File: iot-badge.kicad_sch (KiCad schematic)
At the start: 12 parts, among them J1 USB_C_Receptacle_USB2.0, J11 Conn_01x01_Male, J12 Conn_01x01_Male, SW1 SW_Push, SW2 SW_Push, SW3 SW_Push, SW4 SW_Push, SW5 SW_Push, SW6 SW_Push, U1 ESP32-WROOM-32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

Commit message: started readme
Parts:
- BT1: footprint Battery:BatteryHolder_Keystone_3009_1x2450 -> Battery:BatteryHolder_Keystone_1057_1x2032
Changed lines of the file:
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@@
       (effects (font (size 1.27 1.27)) (justify left))
     )
-    (property "Footprint" "Battery:BatteryHolder_Keystone_3009_1x2450" (id 2) (at 76.2 108.966 90)
+    (property "Footprint" "Battery:BatteryHolder_Keystone_1057_1x2032" (id 2) (at 76.2 108.966 90)
       (effects (font (size 1.27 1.27)) hide)
     )
@@
   (symbol_instances
     (path "/2b36dd8d-f681-41f9-9d0f-3ba1f06030ee"
-      (reference "BT1") (unit 1) (value "Battery_Cell") (footprint "Battery:BatteryHolder_Keystone_3009_1x2450")
+      (reference "BT1") (unit 1) (value "Battery_Cell") (footprint "Battery:BatteryHolder_Keystone_1057_1x2032")
     )
     (path "/b1b227c3-763e-438d-aed7-d3f1dd332c2c"

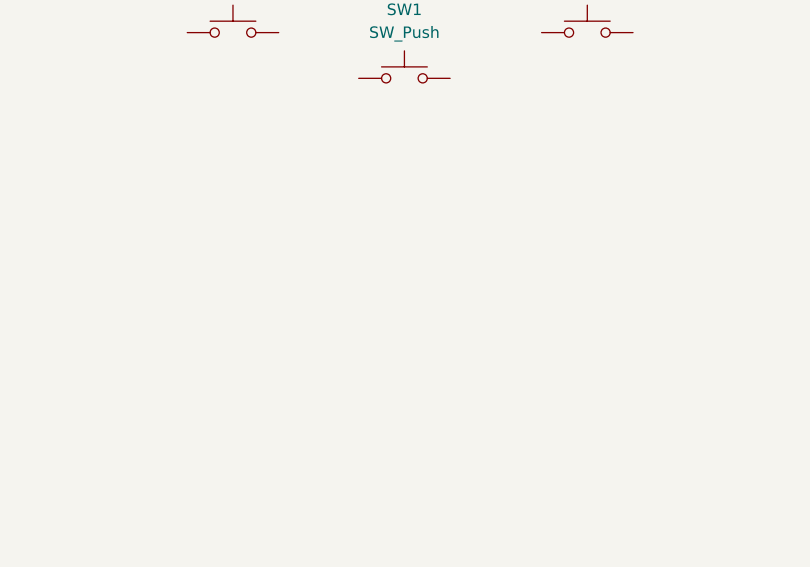
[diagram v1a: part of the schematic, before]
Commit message: pcb antenna finished
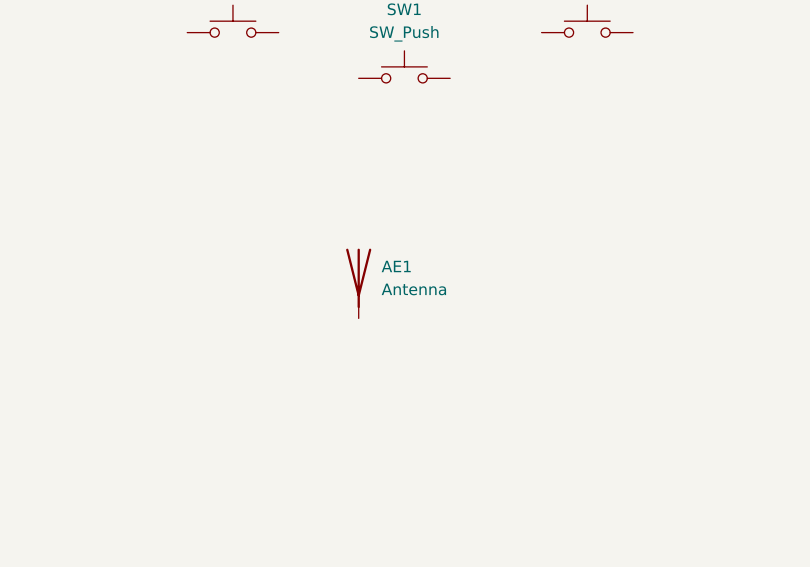
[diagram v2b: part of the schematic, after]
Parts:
- added AE1: Antenna, RF_PCB_Antenna:Micrel_Heli_2, symbol Device:Antenna
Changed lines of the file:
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@@
     (pin "2")
+  )
+  (symbol (lib_id "Device:Antenna") (at 184.15 104.14 0) (unit 1)
+    (in_bom yes) (on_board yes) (fields_autoplaced)
+    (property "Reference" "AE1" (id 0) (at 186.69 103.5049 0)
+      (effects (font (size 1.27 1.27)) (justify left))
+    )
+    (property "Value" "Antenna" (id 1) (at 186.69 106.0449 0)
+      (effects (font (size 1.27 1.27)) (justify left))
+    )
+    (property "Footprint" "RF_PCB_Antenna:Micrel_Heli_2" (id 2) (at 184.15 104.14 0)
+      (effects (font (size 1.27 1.27)) hide)
+    )
+    (property "Datasheet" "~" (id 3) (at 184.15 104.14 0)
+      (effects (font (size 1.27 1.27)) hide)
+    )
+    (pin "1")
   )
   (symbol (lib_id "Switch:SW_Push") (at 256.54 62.23 0) (unit 1)
@@
   )
   (symbol_instances
+    (path "/17a036a7-3c7d-4750-8cd7-b5f99a19695c"
+      (reference "AE1") (unit 1) (value "Antenna") (footprint "RF_PCB_Antenna:Micrel_Heli_2")
+    )
     (path "/2b36dd8d-f681-41f9-9d0f-3ba1f06030ee"
       (reference "BT1") (unit 1) (value "Battery_Cell") (footprint "Battery:BatteryHolder_Keystone_1057_1x2032")

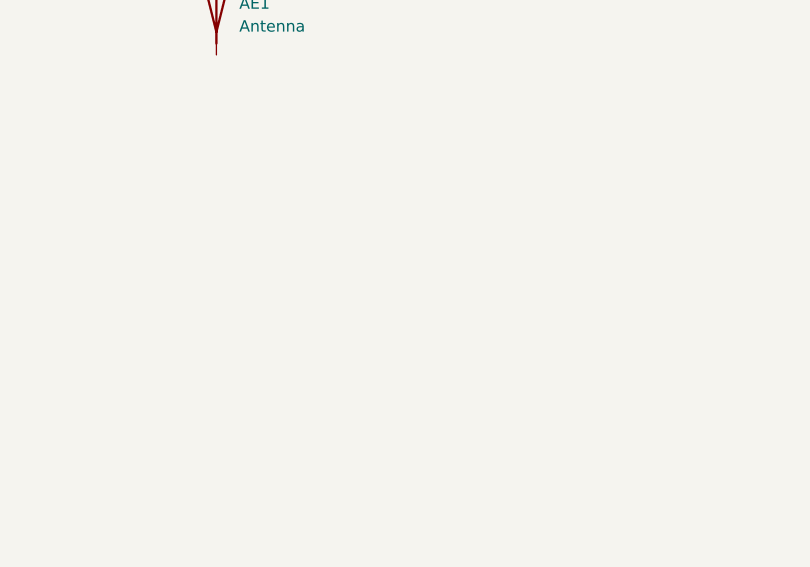
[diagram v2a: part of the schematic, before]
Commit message: i2c display footprint started
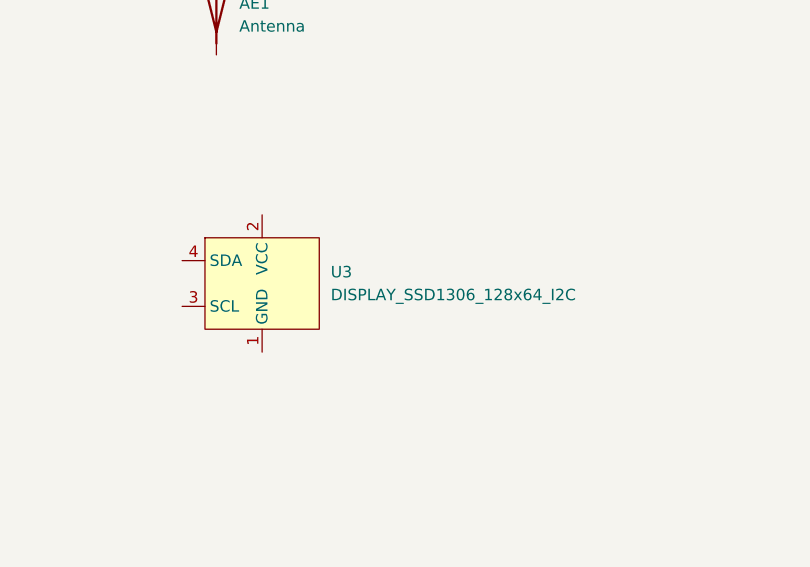
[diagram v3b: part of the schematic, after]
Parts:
- added U3: DISPLAY_SSD1306_128x64_I2C, Display_PCB:DISPLAY_SSD1306_128x64_I2C_0.96inch, symbol Display_PCB:DISPLAY_SSD1306_128x64_I2C
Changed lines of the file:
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@@
     (pin "S1")
+  )
+  (symbol (lib_id "Display_PCB:DISPLAY_SSD1306_128x64_I2C") (at 189.23 134.62 0) (unit 1)
+    (in_bom yes) (on_board yes) (fields_autoplaced)
+    (property "Reference" "U3" (id 0) (at 196.85 133.3499 0)
+      (effects (font (size 1.27 1.27)) (justify left))
+    )
+    (property "Value" "DISPLAY_SSD1306_128x64_I2C" (id 1) (at 196.85 135.8899 0)
+      (effects (font (size 1.27 1.27)) (justify left))
+    )
+    (property "Footprint" "Display_PCB:DISPLAY_SSD1306_128x64_I2C_0.96inch" (id 2) (at 189.23 134.62 0)
+      (effects (font (size 1.27 1.27)) hide)
+    )
+    (property "Datasheet" "" (id 3) (at 189.23 134.62 0)
+      (effects (font (size 1.27 1.27)) hide)
+    )
+    (pin "1")
+    (pin "2")
+    (pin "3")
+    (pin "4")
   )
   (symbol (lib_id "Switch:SW_Push") (at 170.18 77.47 0) (unit 1)
@@
       (reference "U2") (unit 1) (value "Ai-Thinker-Ra-02") (footprint "RF_Module:Ai-Thinker-Ra-01-LoRa")
     )
+    (path "/c4679b10-bd4b-48ad-87a1-2082ffb3234c"
+      (reference "U3") (unit 1) (value "DISPLAY_SSD1306_128x64_I2C") (footprint "Display_PCB:DISPLAY_SSD1306_128x64_I2C_0.96inch")
+    )
   )

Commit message: improved holding holes
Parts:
- SW1, SW2, SW3, SW4, SW5, SW6: footprint Button_Switch_THT:SW_PUSH_6mm -> Button_Switch_SMD:SW_Push_1P1T_NO_6x6mm_H9.5mm
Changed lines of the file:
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@@
     (property "Reference" "SW1" (id 0) (at 189.23 74.93 0))
     (property "Value" "SW_Push" (id 1) (at 189.23 77.47 0))
-    (property "Footprint" "Button_Switch_THT:SW_PUSH_6mm" (id 2) (at 189.23 77.47 0)
+    (property "Footprint" "Button_Switch_SMD:SW_Push_1P1T_NO_6x6mm_H9.5mm" (id 2) (at 189.23 77.47 0)
       (effects (font (size 1.27 1.27)) hide)
     )
@@
     (property "Reference" "SW5" (id 0) (at 256.54 54.61 0))
     (property "Value" "SW_Push" (id 1) (at 256.54 57.15 0))
-    (property "Footprint" "Button_Switch_THT:SW_PUSH_6mm" (id 2) (at 256.54 57.15 0)
+    (property "Footprint" "Button_Switch_SMD:SW_Push_1P1T_NO_6x6mm_H9.5mm" (id 2) (at 256.54 57.15 0)
       (effects (font (size 1.27 1.27)) hide)
     )
@@
     (property "Reference" "SW6" (id 0) (at 256.54 66.04 0))
     (property "Value" "SW_Push" (id 1) (at 256.54 68.58 0))
-    (property "Footprint" "Button_Switch_THT:SW_PUSH_6mm" (id 2) (at 256.54 68.58 0)
+    (property "Footprint" "Button_Switch_SMD:SW_Push_1P1T_NO_6x6mm_H9.5mm" (id 2) (at 256.54 68.58 0)
       (effects (font (size 1.27 1.27)) hide)
     )
@@
     (property "Reference" "SW4" (id 0) (at 209.55 69.85 0))
     (property "Value" "SW_Push" (id 1) (at 209.55 72.39 0))
-    (property "Footprint" "Button_Switch_THT:SW_PUSH_6mm" (id 2) (at 209.55 72.39 0)
+    (property "Footprint" "Button_Switch_SMD:SW_Push_1P1T_NO_6x6mm_H9.5mm" (id 2) (at 209.55 72.39 0)
       (effects (font (size 1.27 1.27)) hide)
     )
@@
     (property "Reference" "SW3" (id 0) (at 170.18 69.85 0))
     (property "Value" "SW_Push" (id 1) (at 170.18 72.39 0))
-    (property "Footprint" "Button_Switch_THT:SW_PUSH_6mm" (id 2) (at 170.18 72.39 0)
+    (property "Footprint" "Button_Switch_SMD:SW_Push_1P1T_NO_6x6mm_H9.5mm" (id 2) (at 170.18 72.39 0)
       (effects (font (size 1.27 1.27)) hide)
     )
@@
     (property "Reference" "SW2" (id 0) (at 189.23 63.5 0))
     (property "Value" "SW_Push" (id 1) (at 189.23 66.04 0))
-    (property "Footprint" "Button_Switch_THT:SW_PUSH_6mm" (id 2) (at 189.23 66.04 0)
+    (property "Footprint" "Button_Switch_SMD:SW_Push_1P1T_NO_6x6mm_H9.5mm" (id 2) (at 189.23 66.04 0)
       (effects (font (size 1.27 1.27)) hide)
     )
@@
     )
     (path "/0c62dc8b-b218-44e3-b535-1d9d37793c70"
-      (reference "SW1") (unit 1) (value "SW_Push") (footprint "Button_Switch_THT:SW_PUSH_6mm")
+      (reference "SW1") (unit 1) (value "SW_Push") (footprint "Button_Switch_SMD:SW_Push_1P1T_NO_6x6mm_H9.5mm")
     )
     (path "/eb75a219-1a8f-4df1-840f-96d35b245652"
-      (reference "SW2") (unit 1) (value "SW_Push") (footprint "Button_Switch_THT:SW_PUSH_6mm")
+      (reference "SW2") (unit 1) (value "SW_Push") (footprint "Button_Switch_SMD:SW_Push_1P1T_NO_6x6mm_H9.5mm")
     )
     (path "/c717c938-c25d-4eef-a243-d41907234a66"
-      (reference "SW3") (unit 1) (value "SW_Push") (footprint "Button_Switch_THT:SW_PUSH_6mm")
+      (reference "SW3") (unit 1) (value "SW_Push") (footprint "Button_Switch_SMD:SW_Push_1P1T_NO_6x6mm_H9.5mm")
     )
     (path "/6cd250dc-3816-4ea6-b47c-a4485f14ccae"
-      (reference "SW4") (unit 1) (value "SW_Push") (footprint "Button_Switch_THT:SW_PUSH_6mm")
+      (reference "SW4") (unit 1) (value "SW_Push") (footprint "Button_Switch_SMD:SW_Push_1P1T_NO_6x6mm_H9.5mm")
     )
     (path "/1b6ba9dd-63d3-4d68-83dc-fb28b914993c"
-      (reference "SW5") (unit 1) (value "SW_Push") (footprint "Button_Switch_THT:SW_PUSH_6mm")
+      (reference "SW5") (unit 1) (value "SW_Push") (footprint "Button_Switch_SMD:SW_Push_1P1T_NO_6x6mm_H9.5mm")
     )
     (path "/5c125622-445c-4334-9e6d-ca1d98c5a595"
-      (reference "SW6") (unit 1) (value "SW_Push") (footprint "Button_Switch_THT:SW_PUSH_6mm")
+      (reference "SW6") (unit 1) (value "SW_Push") (footprint "Button_Switch_SMD:SW_Push_1P1T_NO_6x6mm_H9.5mm")
     )
     (path "/ef77c8d4-ce08-4ef5-b188-2b769cbf3a7c"

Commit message: changed battery for AAA
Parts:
- BT1: footprint Battery:BatteryHolder_Keystone_1057_1x2032 -> Battery:BatteryHolder_Keystone_2466_1xAAA
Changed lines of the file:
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@@
       (effects (font (size 1.27 1.27)) (justify left))
     )
-    (property "Footprint" "Battery:BatteryHolder_Keystone_1057_1x2032" (id 2) (at 76.2 108.966 90)
+    (property "Footprint" "Battery:BatteryHolder_Keystone_2466_1xAAA" (id 2) (at 76.2 108.966 90)
       (effects (font (size 1.27 1.27)) hide)
     )
@@
     )
     (path "/2b36dd8d-f681-41f9-9d0f-3ba1f06030ee"
-      (reference "BT1") (unit 1) (value "Battery_Cell") (footprint "Battery:BatteryHolder_Keystone_1057_1x2032")
+      (reference "BT1") (unit 1) (value "Battery_Cell") (footprint "Battery:BatteryHolder_Keystone_2466_1xAAA")
     )
     (path "/b1b227c3-763e-438d-aed7-d3f1dd332c2c"

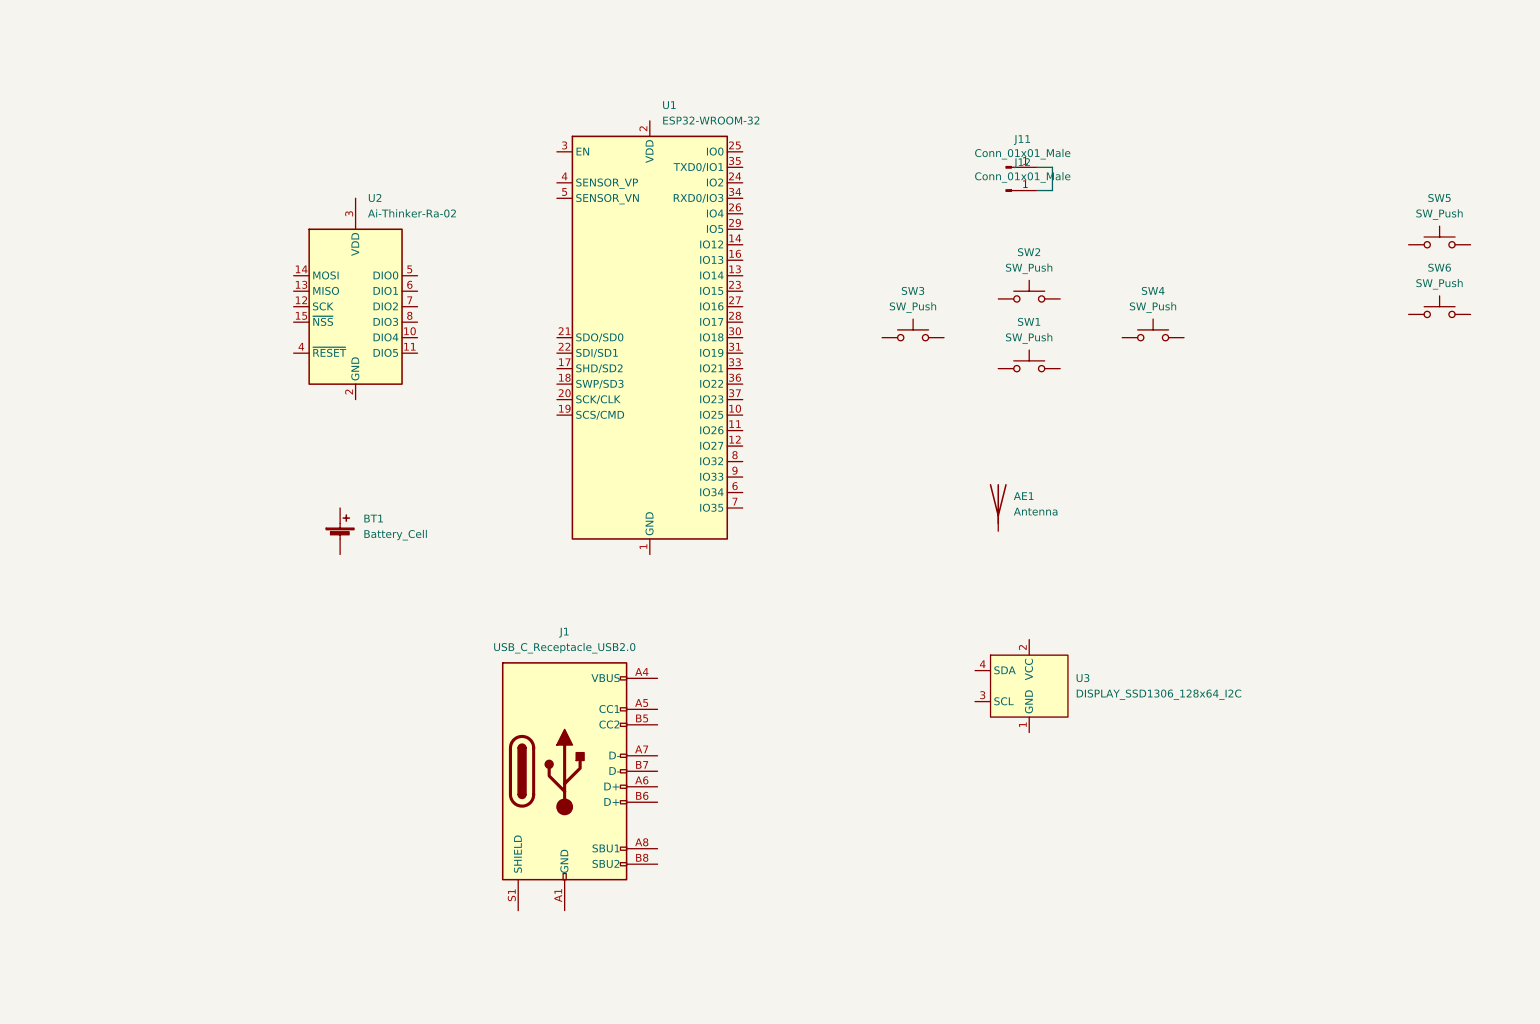
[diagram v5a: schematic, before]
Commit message: added some USB components
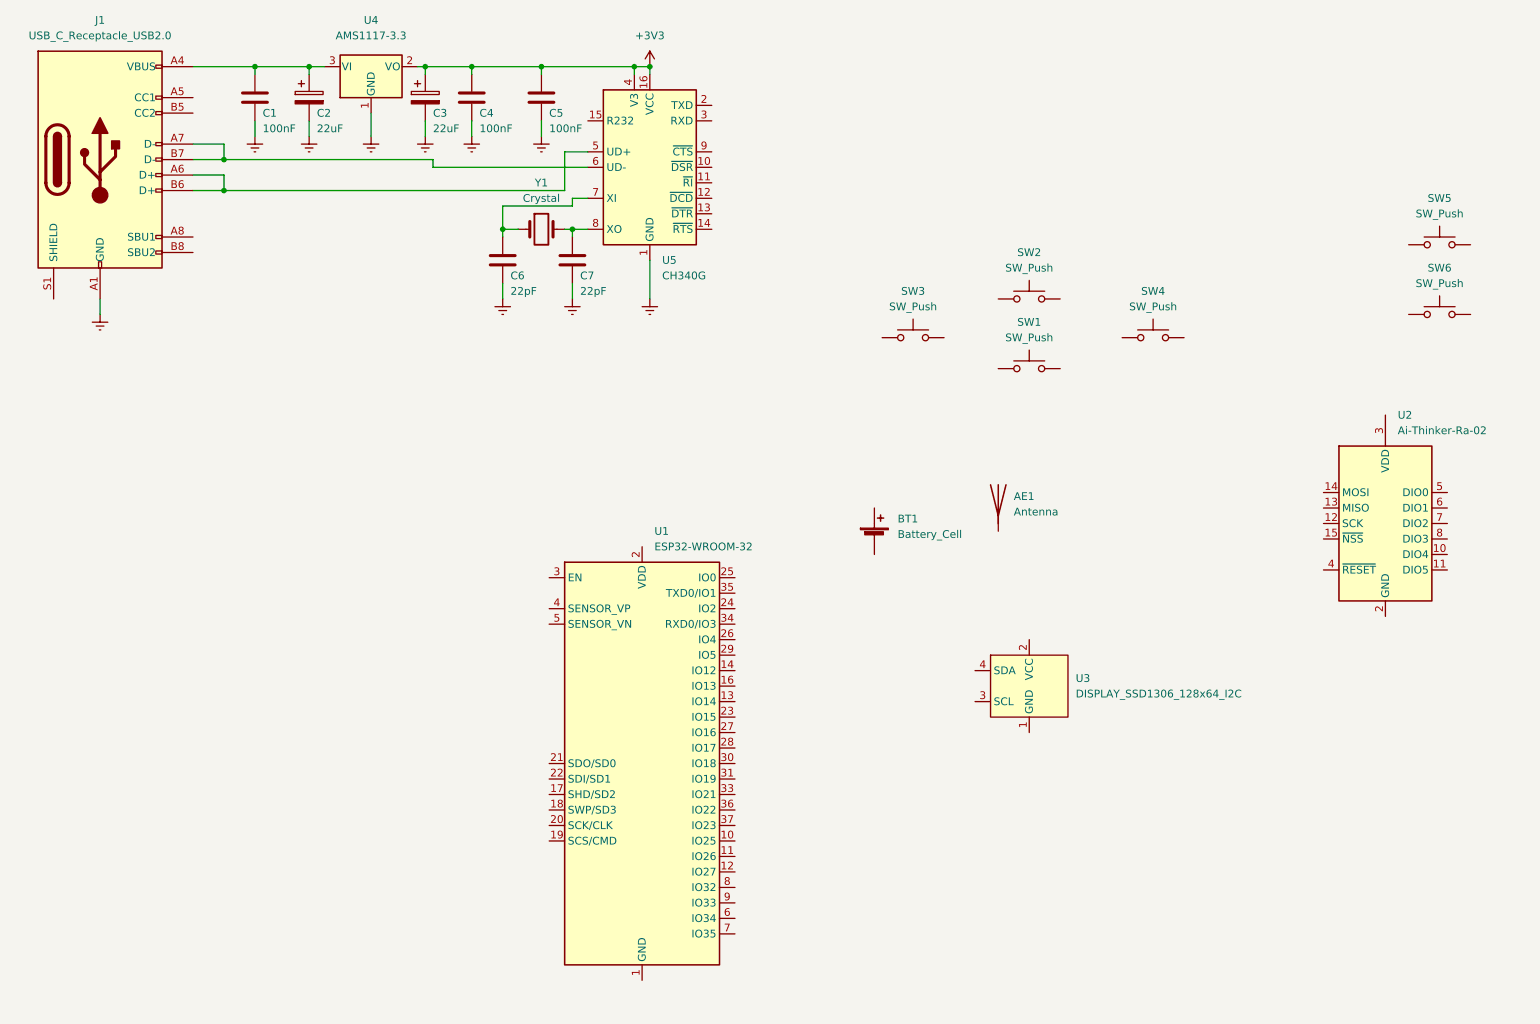
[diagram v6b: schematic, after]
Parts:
- removed J11, J12: Conn_01x01_Male, Connector_Wire:SolderWirePad_1x01_Drill0.8mm, symbol Connector:Conn_01x01_Male
- added C1, C4, C5: 100nF, Capacitor_SMD:C_0805_2012Metric_Pad1.18x1.45mm_HandSolder, symbol Device:C
- added C2, C3: 22uF, Capacitor_Tantalum_SMD:CP_EIA-2012-15_AVX-P_Pad1.30x1.05mm_HandSolder, symbol Device:C_Polarized
- added C6, C7: 22pF, Capacitor_SMD:C_0805_2012Metric_Pad1.18x1.45mm_HandSolder, symbol Device:C
- added U4: AMS1117-3.3, Package_TO_SOT_SMD:SOT-223-3_TabPin2, symbol Regulator_Linear:AMS1117-3.3
- added U5: CH340G, Package_SO:SOIC-16_3.9x9.9mm_P1.27mm, symbol Interface_USB:CH340G
- added Y1: Crystal, Crystal:Crystal_SMD_0603-2Pin_6.0x3.5mm_HandSoldering, symbol Device:Crystal
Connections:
- net Earth: now reaches J1.A1 (GND), J1.A12 (GND), J1.B1 (GND), J1.B12 (GND)
- net Earth: now also C1.2, C2.2, C3.2, C4.2, C5.2, C6.2, C7.2, U4.1 (GND), U5.1 (GND)
- net at J1.A4 (VBUS), J1.A9 (VBUS), J1.B4 (VBUS)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: now also C1.1, C2.1, U4.3 (VI)
- net at J1.A6 (D+): now also J1.B6 (D+), U5.5 (UD+)
- net at J1.A7 (D-): now also J1.B7 (D-), U5.6 (UD-)
- new net: C6.1, U5.7 (XI), Y1.1
- new net: C7.1, U5.8 (XO), Y1.2
- new net +3V3: C3.1, C4.1, C5.1, U4.2 (VO), U5.16 (VCC), U5.4 (V3)
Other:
- moved on the sheet: BT1, J1, U1, U2

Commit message: ant needs some care NETS
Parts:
- added C8: 100nF, Capacitor_SMD:C_0805_2012Metric_Pad1.18x1.45mm_HandSolder, symbol Device:C
- added Q1, Q2: BC847, Package_TO_SOT_SMD:SOT-23, symbol Transistor_BJT:BC847
- added R1, R2, R3: 10k, Resistor_SMD:R_0805_2012Metric_Pad1.20x1.40mm_HandSolder, symbol Device:R
- AE1: value Antenna -> Antenna 433
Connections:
- net +3V3: now also U1.2 (VDD), R1.1
- net Earth: now also U1.1 (GND), U1.15 (GND), U1.38 (GND), U1.39 (GND), C8.2
- net at AE1.1 (A): now also U2.14 (MOSI)
- net IO0: now reaches U5.13 (~{DTR})
- net IO0: now also U1.25 (IO0), Q2.2 (E), R2.2
- net at U5.14 (~{RTS}): now also Q1.2 (E), R3.2
- net EN: now reaches U1.3 (EN)
- net EN: now also C8.1, Q1.3 (C), R1.2
- new net: Q2.1 (B), R3.1
- new net: Q1.1 (B), R2.1
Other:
- moved on the sheet: SW1, SW2, SW3, SW4
